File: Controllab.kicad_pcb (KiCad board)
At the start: 2 copper layers, 56.5 x 70 mm, 57 parts, among them J3 TYPE-C-31-M-12, SW1 SW_Push, SW2 SW_Push, U2 ESP32-S3-MINI-1, U3 PN5321A3HN_C1xx, U4 AMS1117-3.3, Y1 Crystal

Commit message: La carte est prete
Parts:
- removed TP1_antenne1, TP2_antenne1: TestPoint, TestPoint:TestPoint_Pad_D1.0mm
- added H1: MountingHole, MountingHole:MountingHole_2.1mm, F.Cu at (140.8, 95.4)
- added H2: MountingHole, MountingHole:MountingHole_2.1mm, F.Cu at (84.5, 95.4)
- added H3: MountingHole, MountingHole:MountingHole_2.1mm, F.Cu at (84.4, 153.5)
- added H4: MountingHole, MountingHole:MountingHole_2.1mm, F.Cu at (141.2, 153.3)
- added J1: BM02B-GHS-TBT_LF__SN__N_, connecteur_pretty:JST_BM02B-GHS-TBT_LF__SN__N_, F.Cu at (128.3, 117.8)
- added JP5: SolderJumper_3_Open, Jumper:SolderJumper-3_P1.3mm_Open_Pad1.0x1.5mm, F.Cu at (85.5, 118.0)
- added JP6: SolderJumper_3_Open, Jumper:SolderJumper-3_P1.3mm_Open_Pad1.0x1.5mm, F.Cu at (85.5, 123.0)
- R9: value 22K -> 2.7K
- SW1, SW2: footprint Button_Switch_SMD:SW_SPST_TL3342 -> Button_Switch_SMD:SW_SPST_PTS645Sx43SMTR92
- moved ANT2 5.71 mm to (113.6, 101.6)
- moved J3 3.90 mm to (141.5, 145.7)
- moved SW2 2.95 mm to (90.5, 140.9)
- moved D6 2.75 mm to (136.2, 139.2)
- moved R1 2.41 mm to (131.4, 152.3)
- moved R3 1.98 mm to (121.6, 153.3), turned to 0 degrees
- moved SW1 1.74 mm to (91.3, 148.5)
- moved TP2_TX2 1.14 mm to (128.1, 123.4)
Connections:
- C17 pad 2: Net-(C16-Pad2) -> Net-(C17-Pad2)
- C19 pad 1: Net-(C16-Pad2) -> Net-(C17-Pad2)
- RQ1 pad 2: Net-(ANT2-T1) -> Net-(JP5-C)
- RQ2 pad 1: Net-(C16-Pad2) -> Net-(C17-Pad2)
- RQ2 pad 2: Net-(ANT2-T2) -> Net-(JP6-C)
- TP1_TX1 pad 1: Net-(ANT2-T1) -> Net-(JP6-C)
- TP2_TX2 pad 1: Net-(ANT2-T2) -> Net-(JP5-C)
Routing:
- net Net-(ANT2-T1): track 94.1 -> 16.8 mm, vias 4 -> 2
- net Net-(ANT2-T2): track 96.6 -> 24.4 mm
- net Net-(JP5-C): track 0.00 -> 59.1 mm, vias 0 -> 3
- net Net-(JP6-B): track 0.00 -> 41.9 mm
- net Net-(JP5-B): track 0.00 -> 40.9 mm
- net Net-(JP6-C): track 0.00 -> 33.6 mm
- net /USB_D+: track 43.8 -> 56.6 mm, vias 4 -> 2
- net Net-(C17-Pad2): track 0.00 -> 10.3 mm
- net /USB_D-: track 43.2 -> 53.4 mm
- net GND: track 264.0 -> 269.7 mm, vias 8 -> 291
- net VBUS: track 64.3 -> 68.6 mm, vias 2 -> 4
- net Net-(J3-CC1): track 12.1 -> 16.2 mm, vias 2 -> 0
- net Net-(J3-CC2): track 5.14 -> 9.17 mm
- net Net-(D6-A2): track 8.90 -> 11.8 mm
- net /GPIO0: track 68.2 -> 65.7 mm
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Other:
- board size 56.5 x 70 mm -> 61.8 x 70.9 mm

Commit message: ajout des noms sur la carte
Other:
- board text added: "CAMPUS FAB"
- board text added: "FABRIQUE PAR MAMADOU MOUCTAR BA ET ALEXANDRU CARP"
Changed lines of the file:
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@@
 		(layer "Edge.Cuts")
+	)
+	(gr_text "CAMPUS FAB"
+		(at 143.102295 109.1 90)
+		(layer "F.SilkS")
+		(effects
+			(font
+				(size 1 1)
+				(thickness 0.15)
+			)
+			(justify left bottom)
+		)
+	)
+	(gr_text "FABRIQUE PAR \nMAMADOU MOUCTAR BA ET ALEXANDRU CARP\n\n"
+		(at 84.3 132.3 270)
+		(layer "B.SilkS")
+		(effects
+			(font
+				(size 1 1)
+				(thickness 0.15)
+			)
+			(justify left bottom mirror)
+		)
 	)
 	(segment

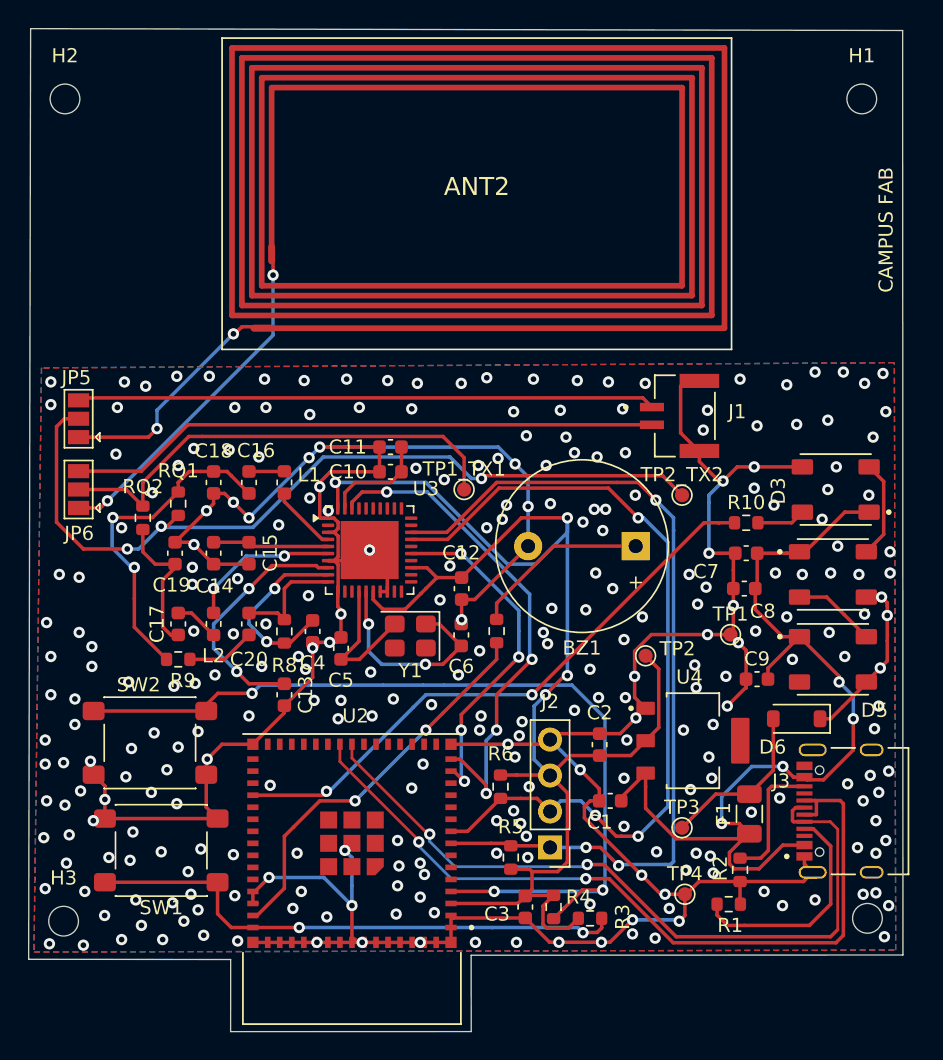
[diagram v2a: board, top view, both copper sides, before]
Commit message: Ajout des noms sur le connecteur de l'oled
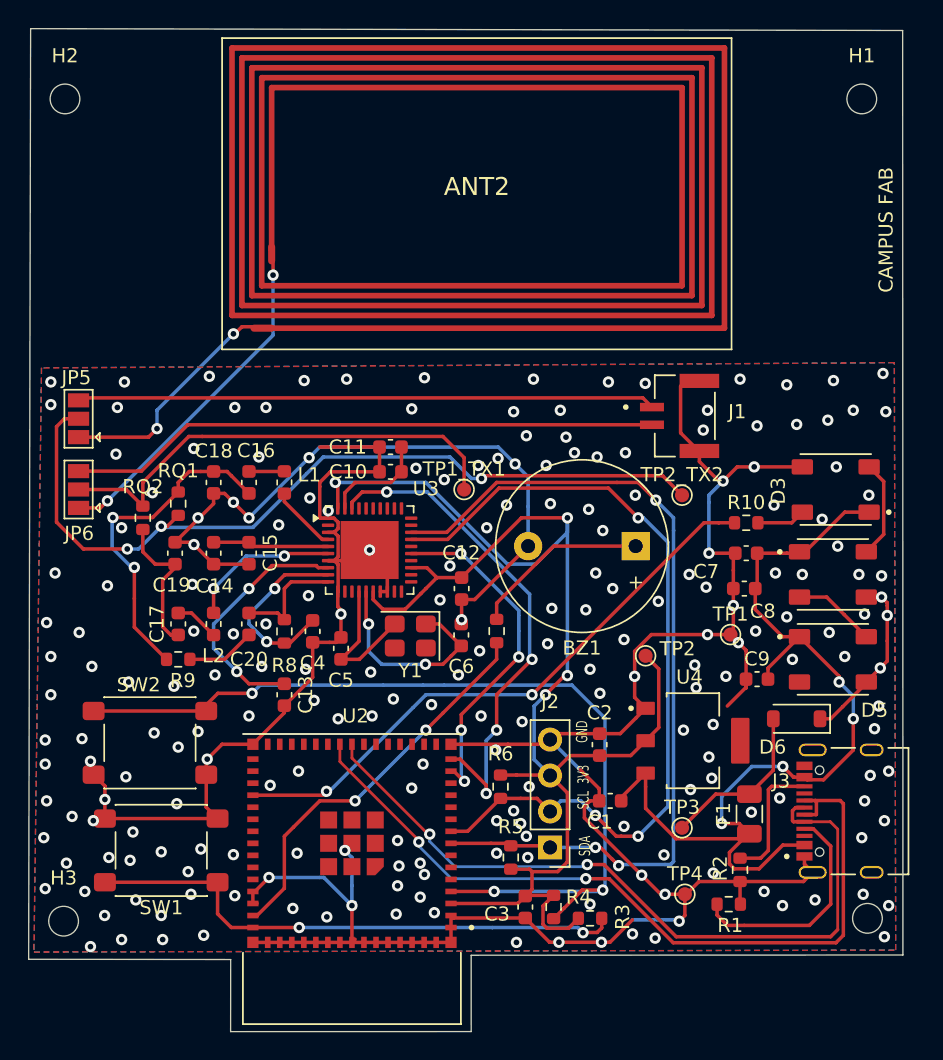
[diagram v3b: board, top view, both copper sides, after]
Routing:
- net GND: track 269.7 -> 269.8 mm, vias 291 -> 221
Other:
- board text added: "3V3"
- board text added: "GND"
- board text added: "SCL"
- board text added: "SDA"
